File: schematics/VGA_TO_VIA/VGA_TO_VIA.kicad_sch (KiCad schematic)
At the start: 10 parts, among them U1 CD74HCT299E, U2 CD74HCT299E, U7 4NAND

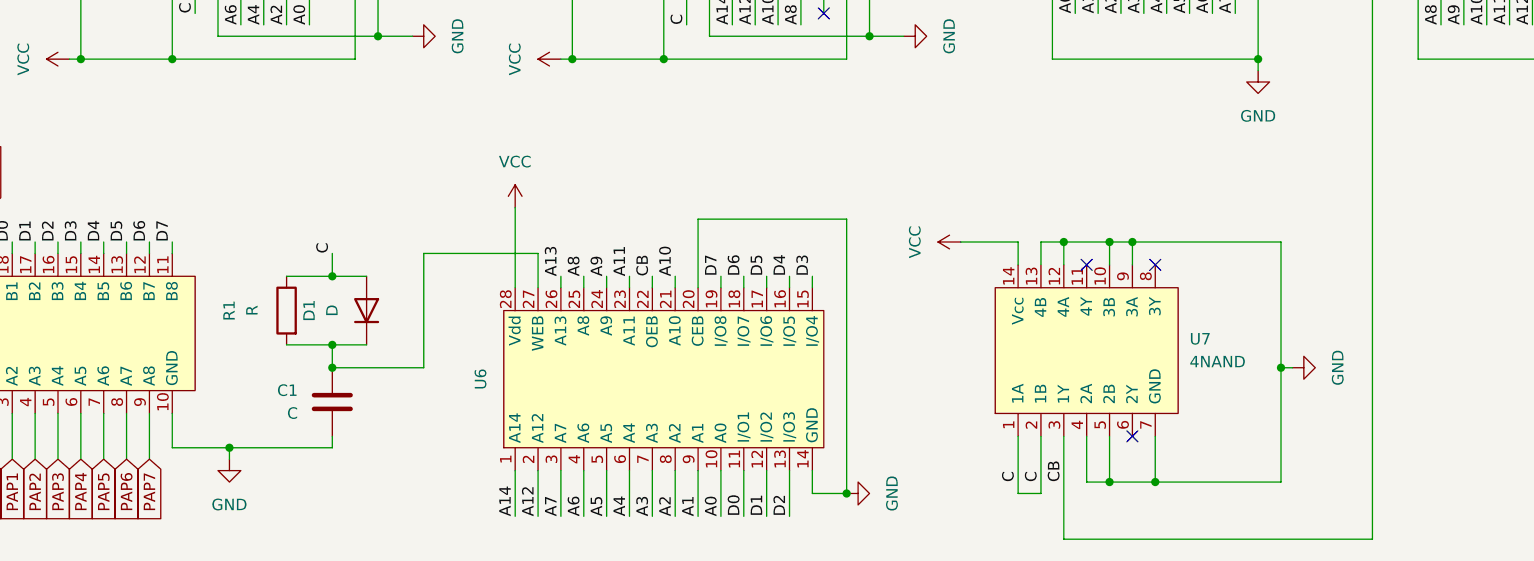
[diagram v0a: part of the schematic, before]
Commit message: Update VGA to VIA delay line
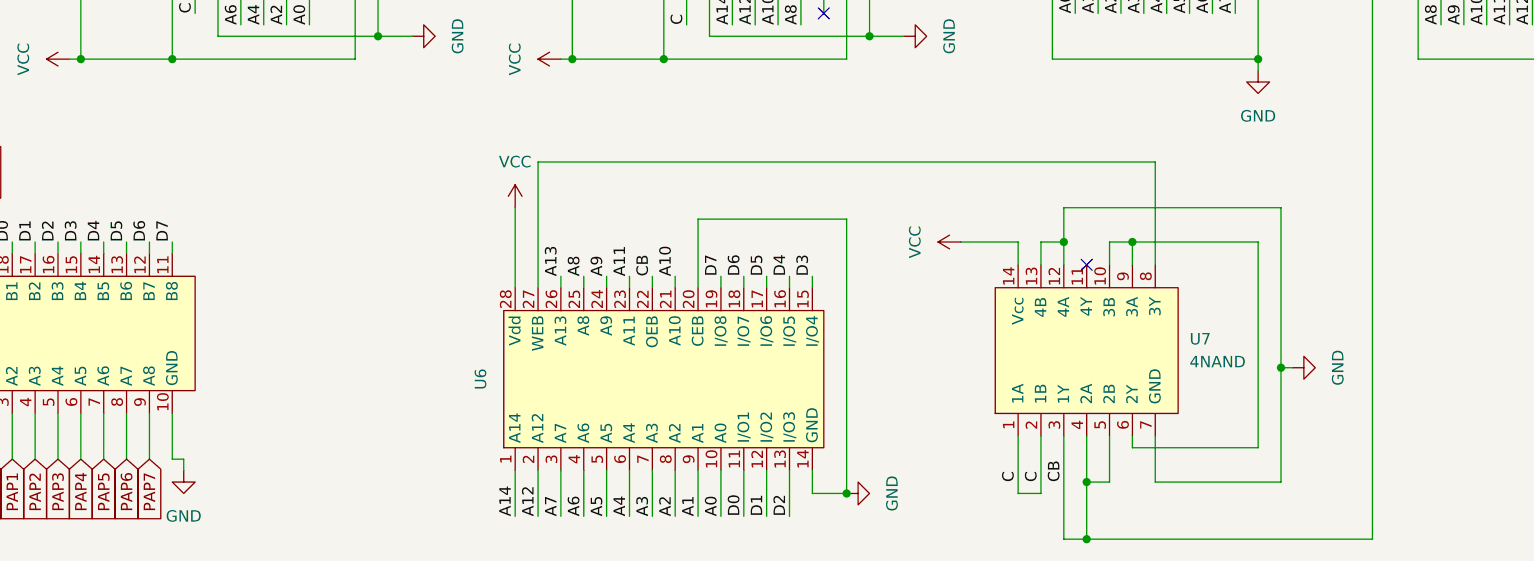
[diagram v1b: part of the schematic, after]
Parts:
- removed C1: C, symbol Device:C
- removed D1: D, symbol Device:D
- removed R1: R, symbol Device:R
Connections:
- net CB: now also U7.4 (2A), U7.5 (2B)
- net GND: no longer U7.10 (3B), U7.4 (2A), U7.5 (2B), U7.9 (3A)
- net at U6.27 (WEB): now also U7.8 (3Y)
- net at U7.6 (2Y): now also U7.10 (3B), U7.9 (3A)
- no-connect marks 10 -> 8
